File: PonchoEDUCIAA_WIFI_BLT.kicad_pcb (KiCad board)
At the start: 2 copper layers, 57.5 x 59.5 mm, 25 parts, among them J1 UART, SW1 Reset, SW2 Boot, U1 ESP32-WROOM

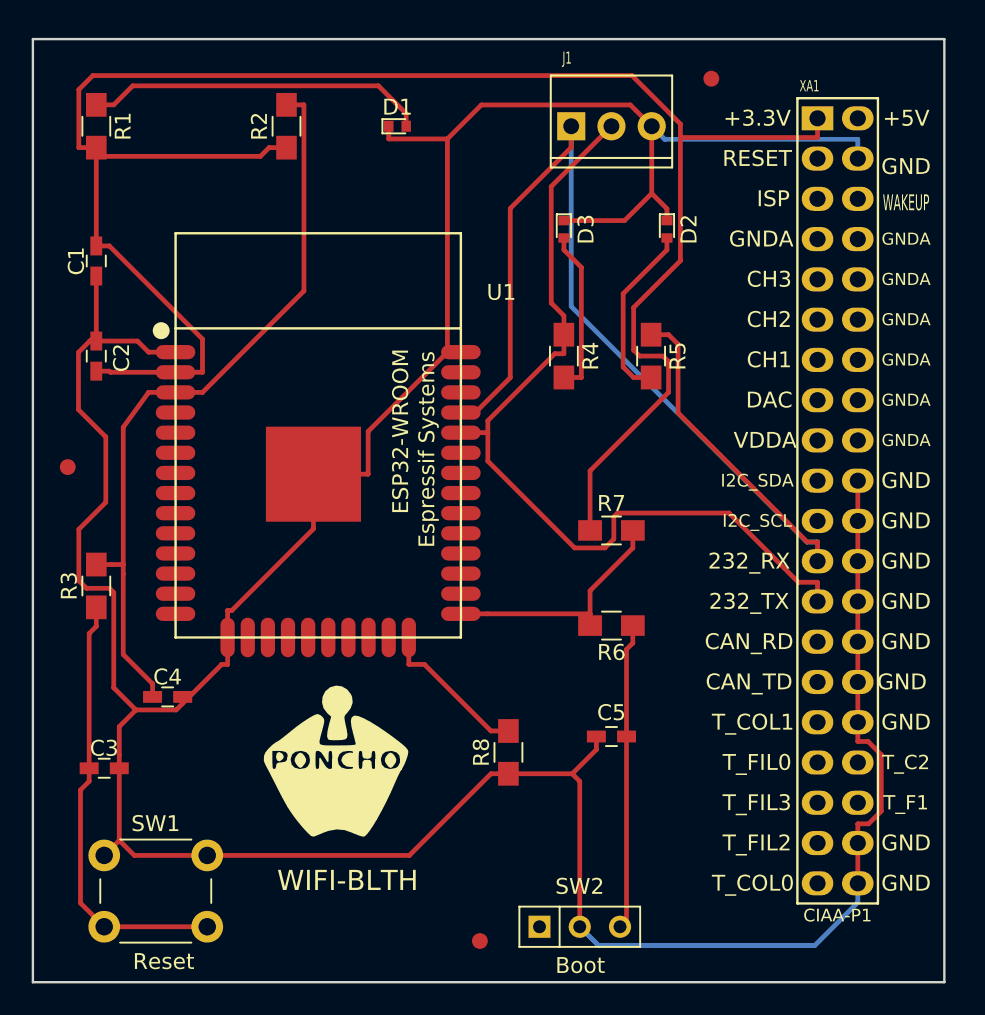
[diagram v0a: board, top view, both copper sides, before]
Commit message: Se cambian los leds, sus datasheets y el footprint para unformizar en 0805 smd
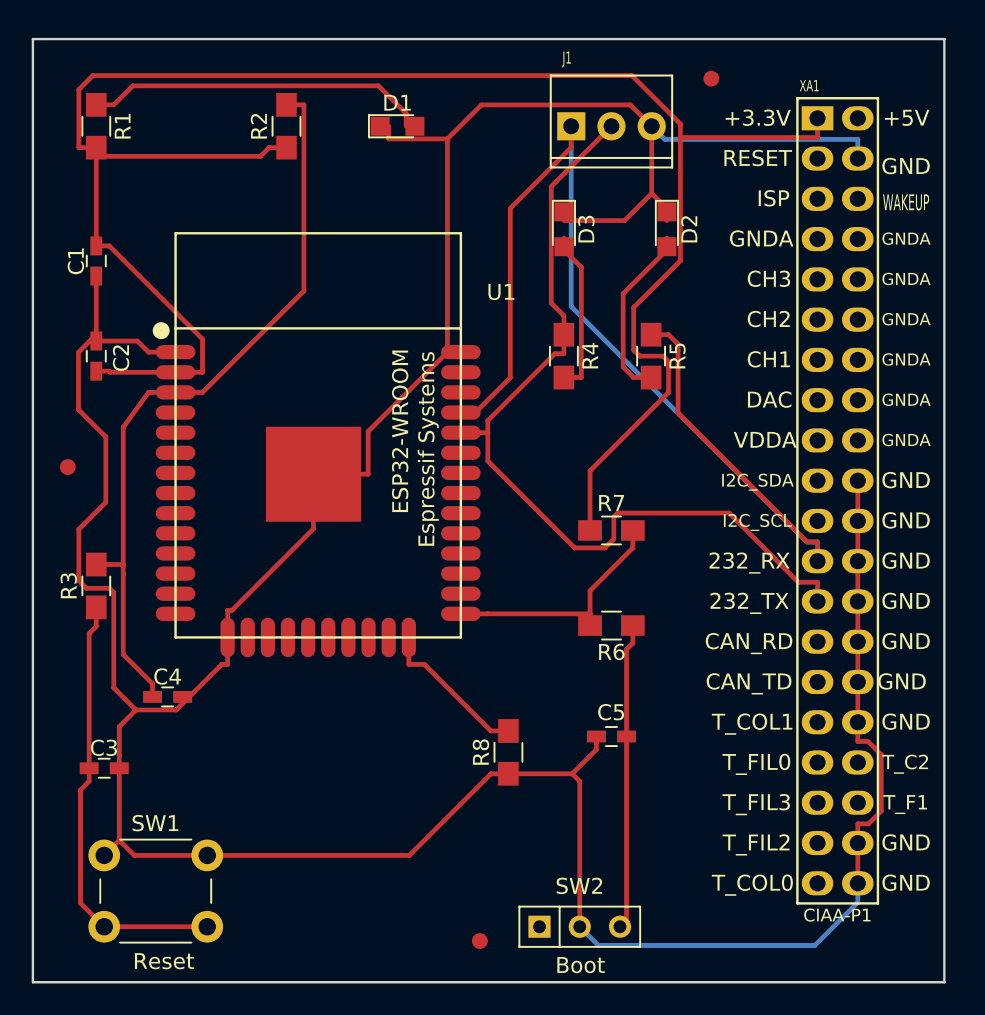
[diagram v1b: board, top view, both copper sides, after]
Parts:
- removed G1: WIFI-BLTH, PonchoEDUCIAA_WIFI_BLTH:Logo_Poncho
- D1, D2, D3: footprint LEDs:LED_0402 -> LEDs:LED_0805

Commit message: Se rehace el placement y el ruteo, se agregan descripciones y zona de cobre.
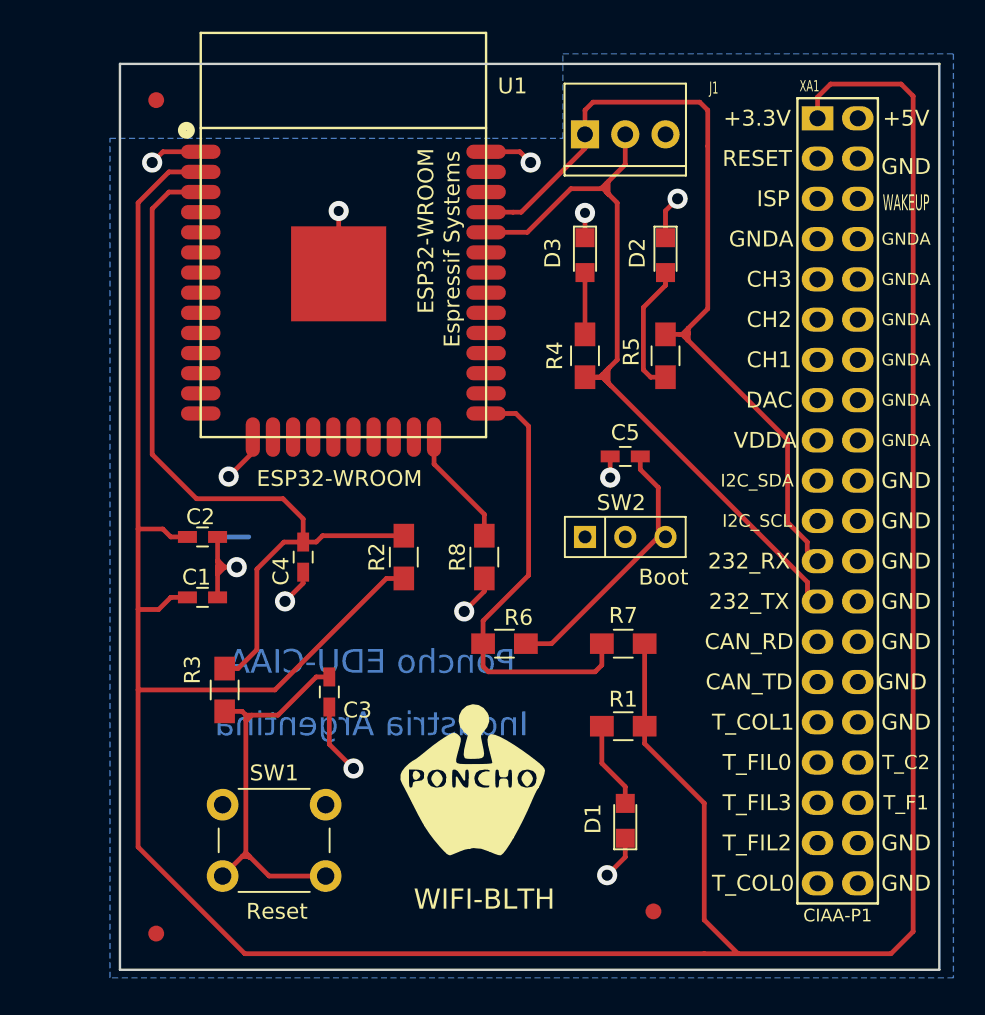
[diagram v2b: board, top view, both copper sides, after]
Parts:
- added G1: WIFI-BLTH, PonchoEDUCIAA_WIFI_BLTH:Logo_Poncho, F.Cu at (156.7, 120.8)
- moved R1 50.4 mm to (166.2, 117.3), turned to 0 degrees
- moved F2 46.4 mm to (168.1, 129.0)
- moved D1 46.1 mm to (166.4, 123.3), turned to 90 degrees
- moved F3 35.0 mm to (136.8, 77.9)
- moved R2 28.2 mm to (152.4, 106.7)
- moved SW2 24.8 mm to (166.4, 105.4)
- moved C1 22.3 mm to (139.7, 109.2), turned to 180 degrees
- moved F1 20.4 mm to (136.8, 130.4)
- moved C5 17.7 mm to (166.4, 100.3)
- moved C3 15.0 mm to (147.7, 115.2), turned to 270 degrees
- moved C2 13.2 mm to (139.7, 105.4), turned to 180 degrees
- moved U1 12.7 mm to (148.6, 86.4)
- moved R8 12.4 mm to (157.5, 106.7)
- moved C4 12.3 mm to (146.1, 106.7), turned to 270 degrees
- moved R3 10.4 mm to (141.1, 115.1)
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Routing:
- net GND: track 234.3 -> 38.0 mm, vias 0 -> 12
- net +3V3: track 121.5 -> 206.8 mm
- net Net-(J1-Pad1): track 75.4 -> 53.7 mm
- net Net-(D1-Pad2): track 21.6 -> 5.48 mm
- net Net-(R6-Pad2): track 15.3 -> 28.5 mm
- net Net-(D3-Pad2): track 10.4 -> 3.90 mm
- net Net-(J1-Pad2): track 54.9 -> 50.7 mm
- net Net-(D2-Pad2): track 11.3 -> 8.31 mm
- net Net-(C3-Pad1): track 27.7 -> 25.2 mm
- net Net-(R8-Pad2): track 9.72 -> 7.54 mm
- net Net-(C5-Pad2): track 19.3 -> 17.1 mm
- net Net-(C4-Pad1): track 47.5 -> 49.4 mm
- net (no net): track 0.00 -> 1.65 mm
- added copper zone on B.Cu, net GND
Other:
- board size 57.5 x 59.5 mm -> 51.7 x 57.2 mm
- rule via_min_size: 0.8 -> 0.7
- board text added: "Aguj. 0,7mm"
- board text added: "ESP32-WROOM"
- board text added: "Grilla pos 5,0 mils"
- board text added: "Industria Argentina"
- board text added: "Pista 0,3 mm"
- board text added: "Poncho EDU-CIAA"
- board text added: "Vía 1,27 mm"

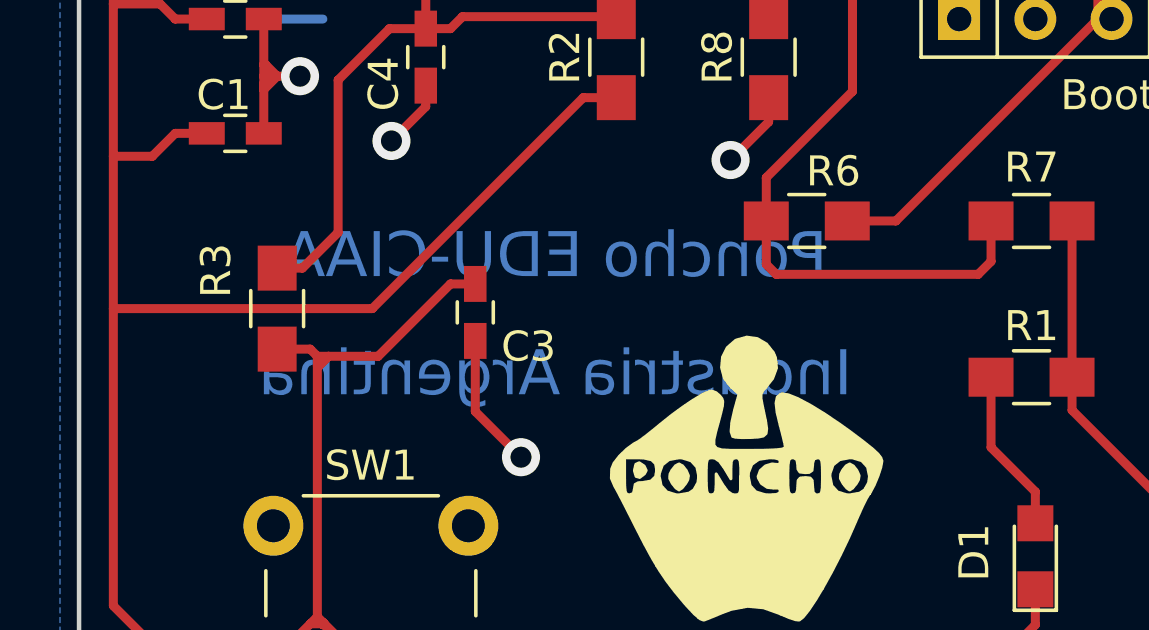
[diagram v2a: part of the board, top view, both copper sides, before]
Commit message: Se mejora el pcb y la vist 3d. Se actualizan los costos con kicost. Se agrega tutorial FreeRouting
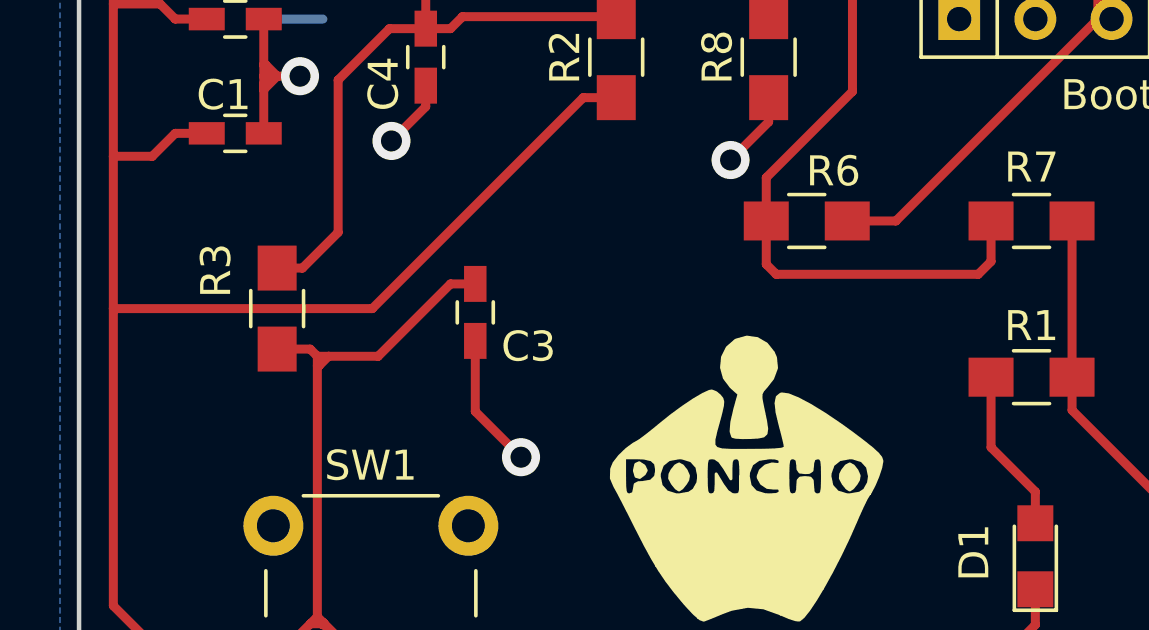
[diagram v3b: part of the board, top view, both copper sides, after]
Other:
- board text added: "Grilla pos 5,0 mils Pista 0,3 mm Vía 1,27 mm Aguj. 0,7 mm"
- board text added: "Poncho EDU-CIAA Industria Argentina"
- board text removed: "Aguj. 0,7mm"
- board text removed: "Grilla pos 5,0 mils"
- board text removed: "Industria Argentina"
- board text removed: "Pista 0,3 mm"
- board text removed: "Poncho EDU-CIAA"
- board text removed: "Vía 1,27 mm"
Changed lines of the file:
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@@
     (area 134.417999 75.489999 186.257001 132.790001)
     (thickness 1.6)
-    (drawings 19)
+    (drawings 16)
     (tracks 204)
     (zones 0)
@@
     (38 B.Mask user)
     (39 F.Mask user)
+    (40 Dwgs.User user)
     (44 Edge.Cuts user)
-    (45 Margin user)
     (46 B.CrtYd user)
+    (47 F.CrtYd user)
     (48 B.Fab user)
     (49 F.Fab user)
@@
       (xy 3.778435 -0.1467) (xy 3.778435 -0.1467)) (layer F.SilkS) (width 0.1))
   )
+  (gr_text "Poncho EDU-CIAA\nIndustria Argentina" (at 150.749 115.189) (layer B.SilkS)
+    (effects (font (size 1.5 1.5) (thickness 0.3)) (justify mirror))
+  )
+  (gr_line (start 200.787 66.802) (end 200.787 55.626) (angle 90) (layer Dwgs.User) (width 0.2))
+  (gr_line (start 200.787 66.929) (end 200.787 66.802) (angle 90) (layer Dwgs.User) (width 0.2))
+  (gr_line (start 224.282 66.929) (end 200.787 66.929) (angle 90) (layer Dwgs.User) (width 0.2))
+  (gr_line (start 224.282 55.626) (end 224.282 66.929) (angle 90) (layer Dwgs.User) (width 0.2))
+  (gr_line (start 200.787 55.626) (end 224.282 55.626) (angle 90) (layer Dwgs.User) (width 0.2))
+  (gr_text "Grilla pos 5,0 mils\nPista  0,3 mm\nVía 1,27 mm\nAguj. 0,7 mm" (at 201.295 61.341) (layer Dwgs.User)
+    (effects (font (size 1.5 1.5) (thickness 0.3)) (justify left))
+  )
+  (dimension 57.15 (width 0.3) (layer Dwgs.User)
+    (gr_text "57,150 mm" (at 130.476 104.14 90) (layer Dwgs.User)
+      (effects (font (size 1.5 1.5) (thickness 0.3)))
+    )
+    (feature1 (pts (xy 134.493 75.565) (xy 129.126 75.565)))
+    (feature2 (pts (xy 134.493 132.715) (xy 129.126 132.715)))
+    (crossbar (pts (xy 131.826 132.715) (xy 131.826 75.565)))
+    (arrow1a (pts (xy 131.826 75.565) (xy 132.412421 76.691504)))
+    (arrow1b (pts (xy 131.826 75.565) (xy 131.239579 76.691504)))
+    (arrow2a (pts (xy 131.826 132.715) (xy 132.412421 131.588496)))
+    (arrow2b (pts (xy 131.826 132.715) (xy 131.239579 131.588496)))
+  )
+  (dimension 51.689 (width 0.3) (layer Dwgs.User)
+    (gr_text "51,689 mm" (at 160.3375 70.913) (layer Dwgs.User)
+      (effects (font (size 1.5 1.5) (thickness 0.3)))
+    )
+    (feature1 (pts (xy 186.182 75.565) (xy 186.182 69.563)))
+    (feature2 (pts (xy 134.493 75.565) (xy 134.493 69.563)))
+    (crossbar (pts (xy 134.493 72.263) (xy 186.182 72.263)))
+    (arrow1a (pts (xy 186.182 72.263) (xy 185.055496 72.849421)))
+    (arrow1b (pts (xy 186.182 72.263) (xy 185.055496 71.676579)))
+    (arrow2a (pts (xy 134.493 72.263) (xy 135.619504 72.849421)))
+    (arrow2b (pts (xy 134.493 72.263) (xy 135.619504 71.676579)))
+  )
   (gr_text Boot (at 168.783 107.95) (layer F.SilkS)
     (effects (font (size 1 1) (thickness 0.15)))
@@
   (gr_text ESP32-WROOM (at 148.336 101.727) (layer F.SilkS)
     (effects (font (size 1 1) (thickness 0.15)))
-  )
-  (gr_line (start 200.152 68.453) (end 200.152 54.864) (angle 90) (layer F.Fab) (width 0.2))
-  (gr_line (start 224.028 68.453) (end 200.152 68.453) (angle 90) (layer F.Fab) (width 0.2))
-  (gr_line (start 224.028 54.864) (end 224.028 68.453) (angle 90) (layer F.Fab) (width 0.2))
-  (gr_line (start 200.279 54.864) (end 224.028 54.864) (angle 90) (layer F.Fab) (width 0.2))
-  (gr_text "Aguj. 0,7mm" (at 208.534 66.294) (layer F.Fab)
-    (effects (font (size 1.5 1.5) (thickness 0.3)))
-  )
-  (gr_text "Vía 1,27 mm" (at 208.661 63.373) (layer F.Fab)
-    (effects (font (size 1.5 1.5) (thickness 0.3)))
-  )
-  (gr_text "Pista 0,3 mm" (at 208.915 59.944) (layer F.Fab)
-    (effects (font (size 1.5 1.5) (thickness 0.3)))
-  )
-  (gr_text "Grilla pos	5,0 mils" (at 211.963 56.642) (layer F.Fab)
-    (effects (font (size 1.5 1.5) (thickness 0.3)))
-  )
-  (dimension 57.15 (width 0.3) (layer F.Fab)
-    (gr_text "57,150 mm" (at 127.682 104.14 90) (layer F.Fab)
-      (effects (font (size 1.5 1.5) (thickness 0.3)))
-    )
-    (feature1 (pts (xy 134.493 75.565) (xy 126.332 75.565)))
-    (feature2 (pts (xy 134.493 132.715) (xy 126.332 132.715)))
-    (crossbar (pts (xy 129.032 132.715) (xy 129.032 75.565)))
-    (arrow1a (pts (xy 129.032 75.565) (xy 129.618421 76.691504)))
-    (arrow1b (pts (xy 129.032 75.565) (xy 128.445579 76.691504)))
-    (arrow2a (pts (xy 129.032 132.715) (xy 129.618421 131.588496)))
-    (arrow2b (pts (xy 129.032 132.715) (xy 128.445579 131.588496)))
-  )
-  (dimension 51.689 (width 0.3) (layer F.Fab)
-    (gr_text "51,689 mm" (at 160.3375 68.5) (layer F.Fab)
-      (effects (font (size 1.5 1.5) (thickness 0.3)))
-    )
-    (feature1 (pts (xy 186.182 75.565) (xy 186.182 67.15)))
-    (feature2 (pts (xy 134.493 75.565) (xy 134.493 67.15)))
-    (crossbar (pts (xy 134.493 69.85) (xy 186.182 69.85)))
-    (arrow1a (pts (xy 186.182 69.85) (xy 185.055496 70.436421)))
-    (arrow1b (pts (xy 186.182 69.85) (xy 185.055496 69.263579)))
-    (arrow2a (pts (xy 134.493 69.85) (xy 135.619504 70.436421)))
-    (arrow2b (pts (xy 134.493 69.85) (xy 135.619504 69.263579)))
   )
   (gr_line (start 134.493 132.715) (end 134.493 75.565) (angle 90) (layer Edge.Cuts) (width 0.15))
@@
   (gr_line (start 186.182 75.565) (end 186.182 132.715) (angle 90) (layer Edge.Cuts) (width 0.15))
   (gr_line (start 134.493 75.565) (end 186.182 75.565) (angle 90) (layer Edge.Cuts) (width 0.15))
-  (gr_text "Poncho EDU-CIAA" (at 150.368 113.284) (layer BOTTOM)
-    (effects (font (size 1.5 1.5) (thickness 0.3)) (justify mirror))
-  )
-  (gr_text "Industria Argentina" (at 150.368 117.221) (layer BOTTOM)
-    (effects (font (size 1.5 1.5) (thickness 0.3)) (justify mirror))
-  )
   (segment (start 140.97 105.41) (end 142.621 105.41) (width 0.3) (layer BOTTOM) (net 0))
   (segment (start 141.097 107.315) (end 140.65 107.762) (width 0.3) (layer TOP) (net 1))
